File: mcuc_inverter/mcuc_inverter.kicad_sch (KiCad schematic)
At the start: 0 parts

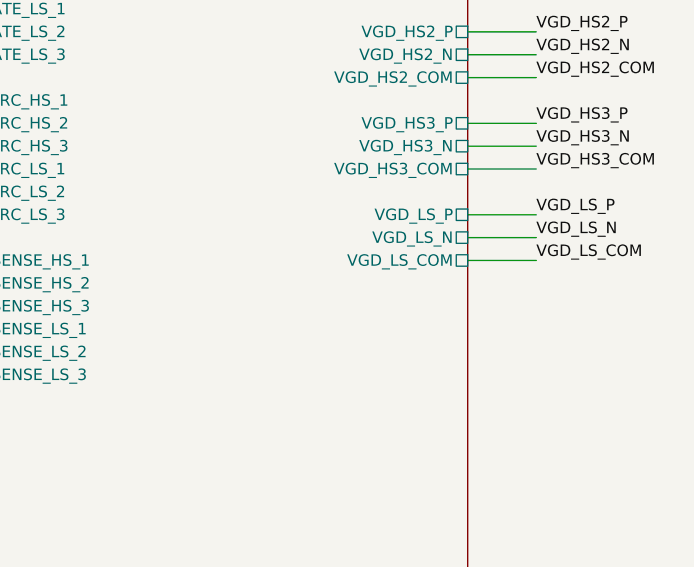
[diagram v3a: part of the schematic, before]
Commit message: Fix gate drive and supervisor: CR-1, CR-2, MJ-1, MJ-8, MJ-9, MJ-13
CR-1 - the fault-clear deadlock is broken. U903 gate 4 now computes
DRV_RST_OUT = DRV_RST_IN AND OC_LATCH_N; FAULT_BKIN is out of the
chain, so a rising RDYC edge is reachable. C907 (220 nF) gives a
1.03 ms power-on clear pulse, comfortably past the drivers' 200 us
start time and the 1.2 us minimum clear width, so the bridge comes
up without firmware intervention. Gate 3 is freed and labelled for
the discharge interlock.

MJ-1 - the overcurrent trip finally reaches TIM1_BKIN. D904 (BAT54WS)
wire-ORs OC_LATCH_N into FAULT_BKIN: 0.33 mA gives 0.31 V against a
0.95 V input-low threshold, and it reverse-biases on driver-only
faults so the two paths stay independent. SPEC 9.2's central claim is
now true as built.

CR-2 - DESAT reconfigured: ADJB linked to VCC1 (LEB 444 ns, filter
263 ns, was 650+1575), ADJA to 28.0k for the family-maximum 699 mA
soft-off, and the external blanking cap DNP'd because the datasheet
specifies all DESAT timing at 2 pF. Chain is now 1.9 us typical
against ~5.8 us before. Worst-case silicon reaches 2.6 us - see the
D026 amendment in the next commit; this is recorded, not rounded.

MJ-8 - added the VCC2-to-VEE2 capacitors that were missing on all six
domains. That is the loop carrying the gate pulse, and the datasheet
explicitly requires it.

MJ-9 - the -5 V off-rail had no defined bias: gate charge nets to zero
at COM, so the zener sat in its knee. 2.49k preloads (6.02 mA) per
isolated domain now hold it defined at 4.87 V, inside the module's
-5 V static maximum.

MJ-13 - LED resistors 100R -> 2.2k and D903 moved ahead of R910. The
fault wire-OR was being back-fed ~11 mA, pushing FAULT_BKIN to 0.94 V
against a 0.99 V threshold; it now sits at ~0.1 V.

MJ-17 - Miller clamp BSS138 -> BSS316N. Note the constraint the agent
found: CLAMPDRV swings to VEE2+11.5 V, so the +-12 V Vgs parts
suggested elsewhere are unusable; this is a +-20 V part.

MN-2 - documentation corrected to the tr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
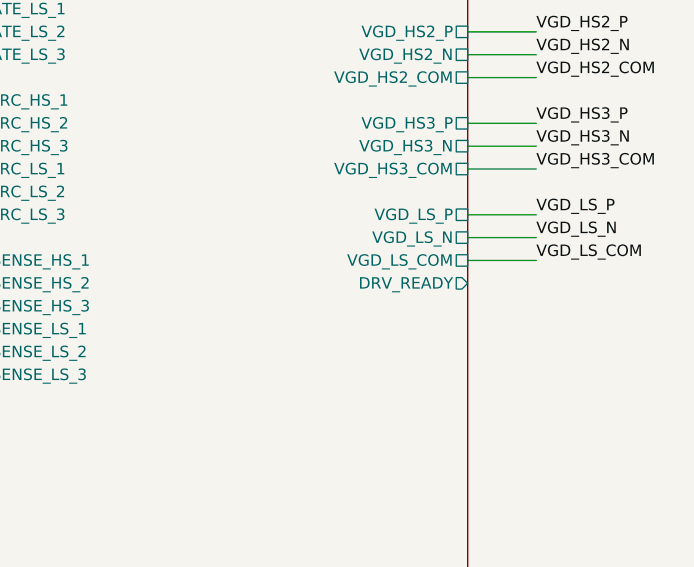
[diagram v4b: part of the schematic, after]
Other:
- sheet Gate drive ports: added DRV_READY; removed none
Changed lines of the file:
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@@
+			)
+		)
+		(pin "DRV_READY" output
+			(at 386.08 78.74 0)
+			(effects
+				(font
+					(size 1.27 1.27)
+				)
+				(justify right)
 			)
 		)

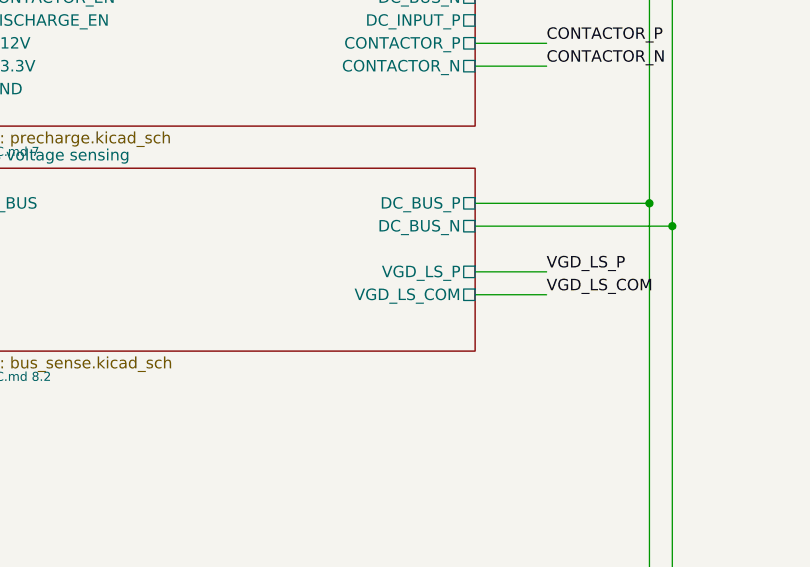
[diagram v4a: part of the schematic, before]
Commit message: CR-3: dedicated isolated supply for the bus-sense amplifier
The AMC1311's high-side LDO had VIN on VGD_LS_P and GND on
VGD_LS_COM - the module's low-side Kelvin-source pins - while its own
output capacitors, the amplifier's GND1 and the divider bottom all
sat on DC_BUS_N. Those are different nets joined only through the
module's internal copper, so at 4 kA/us across ~8 nH of source
inductance tens of volts appeared inside the supply loop every
switching edge, and a Kelvin sense node was carrying power current.

Replaced with the pattern TI actually recommends: an SN6505B
push-pull stage from the LV 5 V rail through a Wuerth 750313734
transformer, rectified and post-regulated to 3.3 V, with everything
on the isolated side referenced to DC_BUS_N. Netlist confirms one
node carrying the LDO ground, all four bypass capacitors, the
divider bottom, the amplifier's GND1 and the transformer's secondary
centre tap.

The transformer is the barrier-crossing element, so it is a genuinely
reinforced part - 800 Vrms/1400 Vpk per IEC62368-1, 5000 Vrms hipot,
9.2 mm creepage - not one of the 2.5 kV-class parts whose hipot
number masks functional-only certification. Its footprint was built
from pad coordinates rendered off the manufacturer drawing and
re-read numerically from the generated file rather than eyeballed.

Root sheet: the now-obsolete VGD_LS_P and VGD_LS_COM pins removed
from the bus_sense sheet symbol. ERC 0 errors.

Sourcing note for the BOM: SN6505BDBVR is on DigiKey backorder at
check; LCSC stocks it.

Co-Authored-By: Claude Fable 5 <noreply@anthropic.com>
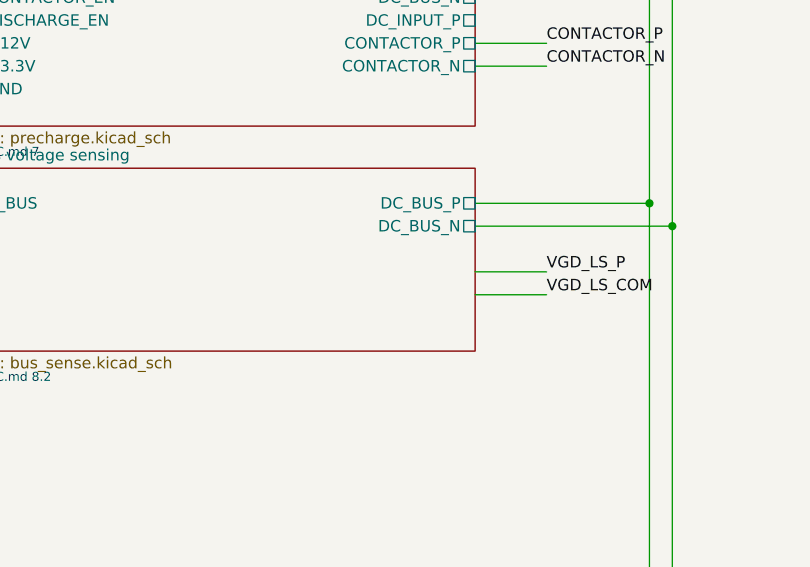
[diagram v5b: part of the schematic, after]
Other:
- sheet Bus voltage sensing ports: added none; removed VGD_LS_COM, VGD_LS_P
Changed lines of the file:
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@@
-			)
-		)
-		(pin "VGD_LS_P" passive
-			(at 75.88 96.52 0)
-			(effects
-				(font
-					(size 1.27 1.27)
-				)
-				(justify left)
-			)
-		)
-		(pin "VGD_LS_COM" passive
-			(at 75.88 99.06 0)
-			(effects
-				(font
-					(size 1.27 1.27)
-				)
-				(justify left)
 			)
 		)

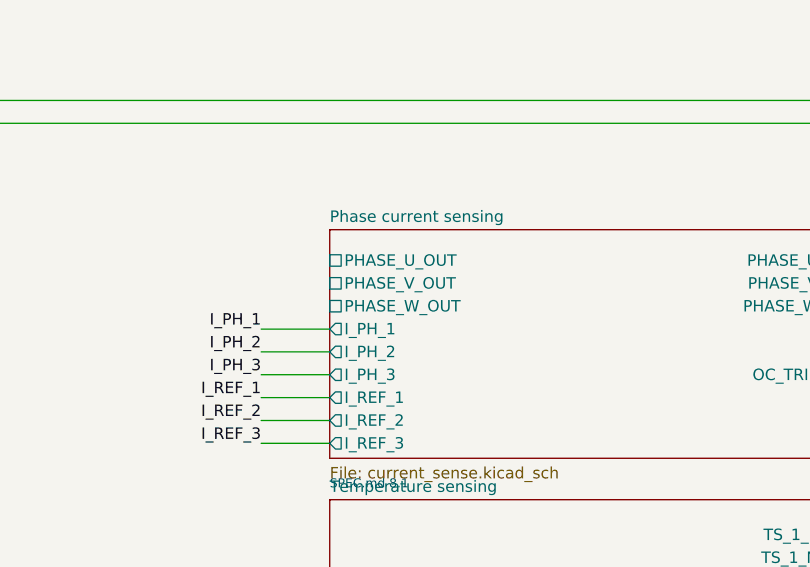
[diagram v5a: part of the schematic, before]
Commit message: Fix precharge, current sense, position, comms per review
Also repairs a library-breaking defect the agent found while working:
the VOM1271T symbol contained a raw newline inside a quoted string,
which silently truncated mcuc_inverter.kicad_sym at parse - every
symbol defined after it was unresolvable. That had been latent since
the symbol was written.

MJ-2/3 - the comparators were wrong twice over: TLV7032 is push-pull
(six of them wire-ORed together plus three open-drain transducer OCD
pins is direct contention), and LM2903's input common-mode range on
3.3 V stops at 1.8 V, below the 2.34 V upper threshold, so the
over-current half could never trip. Now TLV7022DDFR: true open-drain,
rail-to-rail input, 260 ns instead of ~3 us.

MJ-4 - the trip point was really 245-356 A because the thresholds
rode a +-4% rail while the transducer's reference is absolute. Each
phase's window is now servo'd off its own Uref through an OPA376
buffer, so the threshold tracks the sensor: 300 A +-8 A.

MJ-7 - a harness disconnect was not fail-safe: that phase's OCD left
the wire-OR and the input floated. 100k pull-downs make an open
harness read as a large negative current and latch the trip at
power-up, before HV is applied.

MJ-12 - the active discharge can no longer be commanded into a live
bus: SN74LVC1G97 computes DISCHARGE_EN AND NOT(CONTACTOR_EN)
self-contained on the sheet, plus a 10k boot pull-down.

Discharge gate now has a real Miller clamp (BSS138 + 1n + 10k) firing
at V_GS ~1.34 V, below the FET's 1.8 V threshold, in under 15 ns -
the 450 V dv/dt step could previously inject ~4.4 V against a 10M
pull-down and a uA-class photovoltaic turn-off.

Bleeder 18.7k -> 14k (56 k total, 56.4 s to 60 V, meeting the <60 s
requirement it was failing at 75.4 s). Precharge resistor respec'd to
>=65 J. Coil freewheels upsized to ES1G/ES2G with anti-series SMBJ24A
TVS for fast relay release, which forced the coil drivers to 60 V
parts - documented with a 17% margin note.

Position: SinCos f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
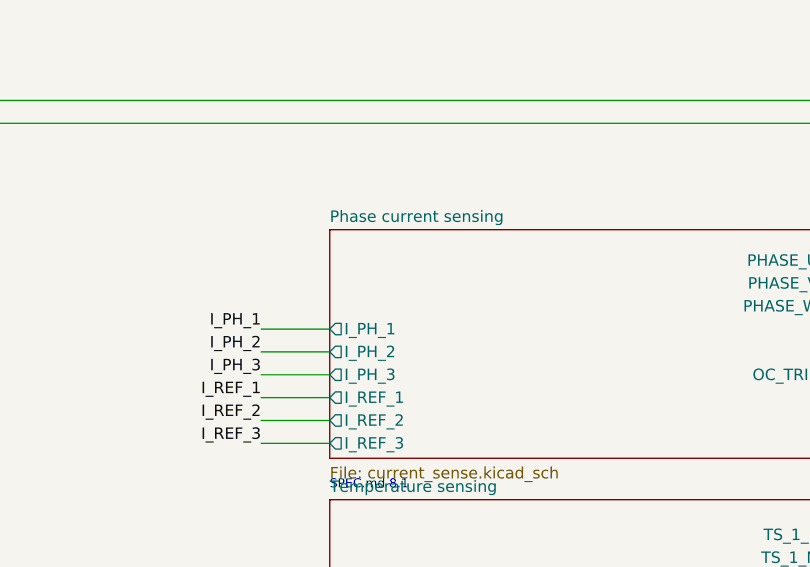
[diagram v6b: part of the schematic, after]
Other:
- sheet Phase current sensing ports: added none; removed PHASE_U_OUT, PHASE_V_OUT, PHASE_W_OUT
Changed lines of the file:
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@@
-			)
-		)
-		(pin "PHASE_U_OUT" passive
-			(at 160.0 58.42 180)
-			(effects
-				(font
-					(size 1.27 1.27)
-				)
-				(justify left)
-			)
-		)
-		(pin "PHASE_V_OUT" passive
-			(at 160.0 60.96 180)
-			(effects
-				(font
-					(size 1.27 1.27)
-				)
-				(justify left)
-			)
-		)
-		(pin "PHASE_W_OUT" passive
-			(at 160.0 63.5 180)
-			(effects
-				(font
-					(size 1.27 1.27)
-				)
-				(justify left)
 			)
 		)
